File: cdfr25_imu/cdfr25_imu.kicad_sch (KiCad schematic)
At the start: 11 parts, among them J1 Conn_01x06_Pin, U1 LSM6DSL, U2 LIS2MDL

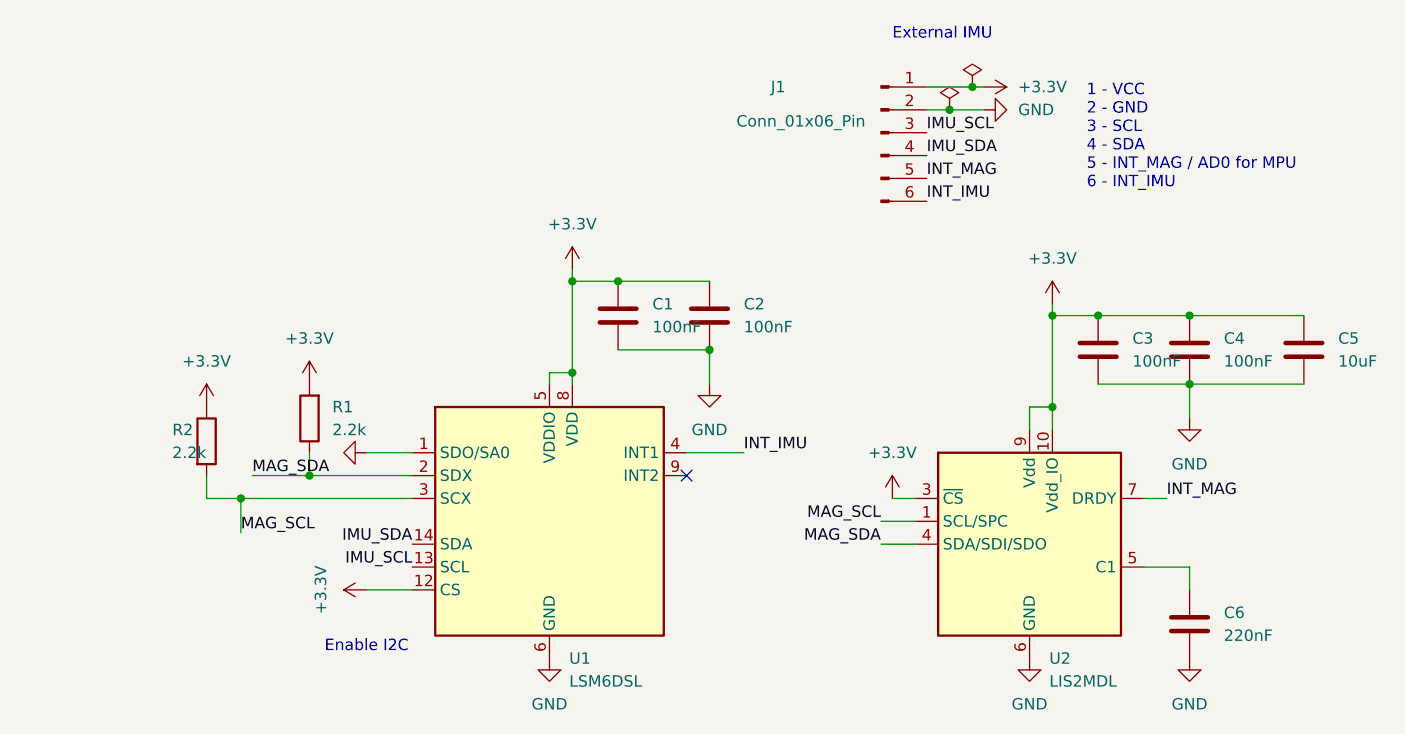
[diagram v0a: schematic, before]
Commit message: Route IMU
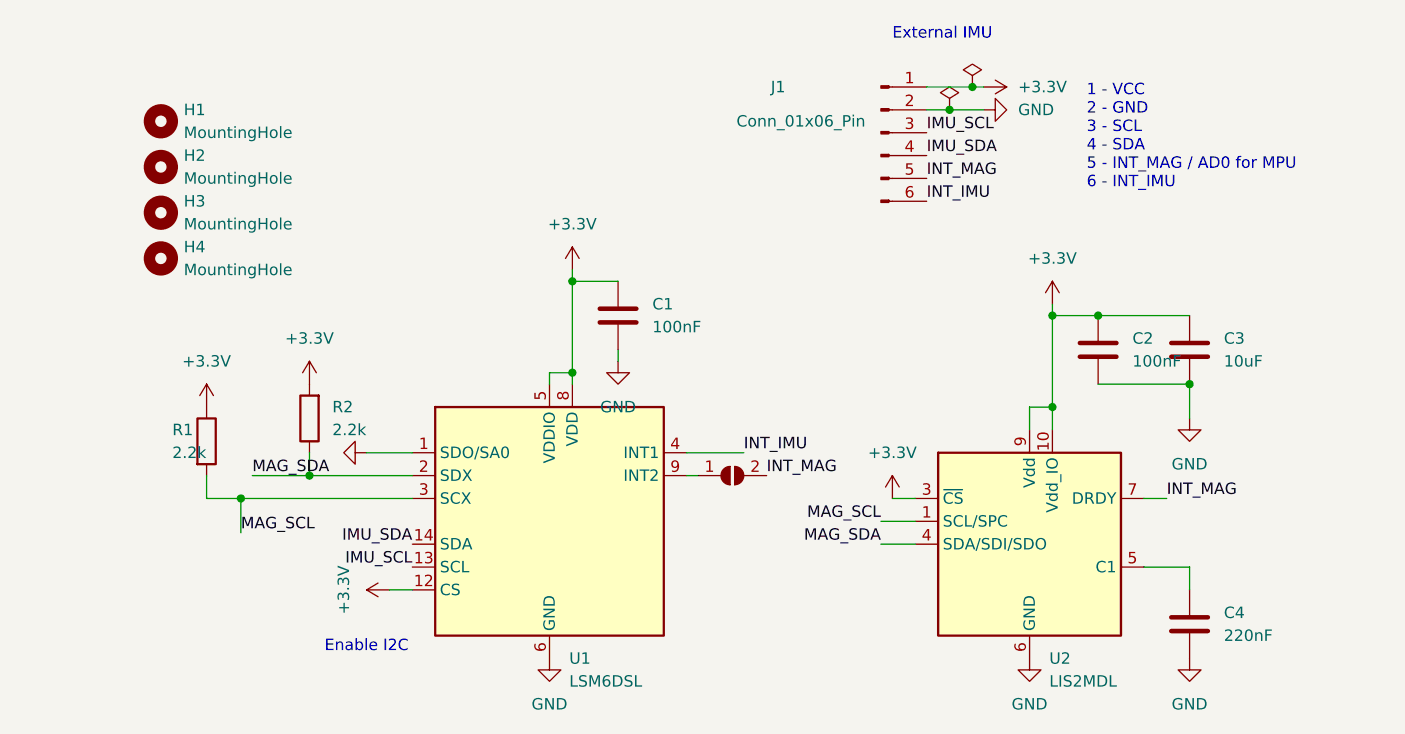
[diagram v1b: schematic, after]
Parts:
- removed C2, C4: 100nF, Capacitor_SMD:C_0805_2012Metric_Pad1.18x1.45mm_HandSolder, symbol Device:C
- added H1, H2, H3, H4: MountingHole, MountingHole:MountingHole_2.2mm_M2, symbol Mechanical:MountingHole
- added JP1: SolderJumper_2_Open, Jumper:SolderJumper-2_P1.3mm_Open_TrianglePad1.0x1.5mm, symbol Jumper:SolderJumper_2_Open
- renumbered C3 to C2, C5 to C3, C6 to C4, R2 to R1, R1 to R2
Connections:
- net INT_MAG: now also JP1.2 (B)
- net at U1.9 (INT2): now also JP1.1 (A)
- no-connect marks 1 -> 0
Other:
- moved on the sheet: C3

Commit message: Add marking
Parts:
- removed H1, H2, H3, H4: MountingHole, MountingHole:MountingHole_2.2mm_M2, symbol Mechanical:MountingHole
- added H1, H2, H3, H4: MountingHole_Pad, MountingHole:MountingHole_2.2mm_M2_Pad_Via, symbol Mechanical:MountingHole_Pad
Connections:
- net GND: now also H1.1, H2.1, H3.1, H4.1
